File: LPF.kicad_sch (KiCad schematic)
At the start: 24 parts

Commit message: v0.6 ERC passes.  I went over it with a fine tooth comb and corrected lots of little stuff.  Ron should review all the components I have to create very carefully.  In particular, MPS-751 symbol does not look correct.
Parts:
- C15: value ? pF -> 47 pF
- C16: value ? pF -> 36 pF
- C4: value ? pF -> 220 pF
- C8: value ? pF -> 100 pF
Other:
- note added: "These are RF paths."
- title: QMX Amp -> QMX+ Amp
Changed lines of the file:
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@@
 	(paper "USLetter")
 	(title_block
-		(title "QMX Amp")
-		(date "2024-08-12")
-		(rev "v0.5")
+		(title "QMX+ Amp")
+		(date "2024-08-13")
+		(rev "v0.6")
 		(company "WA7GIL")
 	)
@@
 		)
 	)
+	(text "These are RF paths."
+		(exclude_from_sim no)
+		(at 21.59 22.098 0)
+		(effects
+			(font
+				(size 1.27 1.27)
+			)
+			(justify left)
+		)
+	)
 	(hierarchical_label "LPF0-OUT"
 		(shape output)
@@
 			)
 		)
-		(property "Value" "? pF"
+		(property "Value" "220 pF"
 			(at 129.54 26.67 90)
 			(effects
@@
 			)
 		)
-		(property "Value" "? pF"
+		(property "Value" "100 pF"
 			(at 129.54 60.96 90)
 			(effects
@@
 			)
 		)
-		(property "Value" "? pF"
+		(property "Value" "47 pF"
 			(at 130.81 95.25 90)
 			(effects
@@
 			)
 		)
-		(property "Value" "? pF"
+		(property "Value" "36 pF"
 			(at 130.81 129.54 90)
 			(effects

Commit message: I think I am working on picking parts
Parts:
- L1, L2, L3, L4, L5, L6, L7, L8: footprint (none) -> ZZZMyLibrary:Toroid_T50_Vertical_L14.0mm_W5.6mm
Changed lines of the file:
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@@
 			)
 		)
-		(property "Footprint" ""
+		(property "Footprint" "ZZZMyLibrary:Toroid_T50_Vertical_L14.0mm_W5.6mm"
 			(at 104.14 76.2 0)
 			(effects
@@
 			)
 		)
-		(property "Footprint" ""
+		(property "Footprint" "ZZZMyLibrary:Toroid_T50_Vertical_L14.0mm_W5.6mm"
 			(at 104.14 41.91 0)
 			(effects
@@
 			)
 		)
-		(property "Footprint" ""
+		(property "Footprint" "ZZZMyLibrary:Toroid_T50_Vertical_L14.0mm_W5.6mm"
 			(at 129.54 76.2 0)
 			(effects
@@
 			)
 		)
-		(property "Footprint" ""
+		(property "Footprint" "ZZZMyLibrary:Toroid_T50_Vertical_L14.0mm_W5.6mm"
 			(at 105.41 144.78 0)
 			(effects
@@
 			)
 		)
-		(property "Footprint" ""
+		(property "Footprint" "ZZZMyLibrary:Toroid_T50_Vertical_L14.0mm_W5.6mm"
 			(at 105.41 110.49 0)
 			(effects
@@
 			)
 		)
-		(property "Footprint" ""
+		(property "Footprint" "ZZZMyLibrary:Toroid_T50_Vertical_L14.0mm_W5.6mm"
 			(at 129.54 41.91 0)
 			(effects
@@
 			)
 		)
-		(property "Footprint" ""
+		(property "Footprint" "ZZZMyLibrary:Toroid_T50_Vertical_L14.0mm_W5.6mm"
 			(at 130.81 110.49 0)
 			(effects
@@
 			)
 		)
-		(property "Footprint" ""
+		(property "Footprint" "ZZZMyLibrary:Toroid_T50_Vertical_L14.0mm_W5.6mm"
 			(at 130.81 144.78 0)
 			(effects

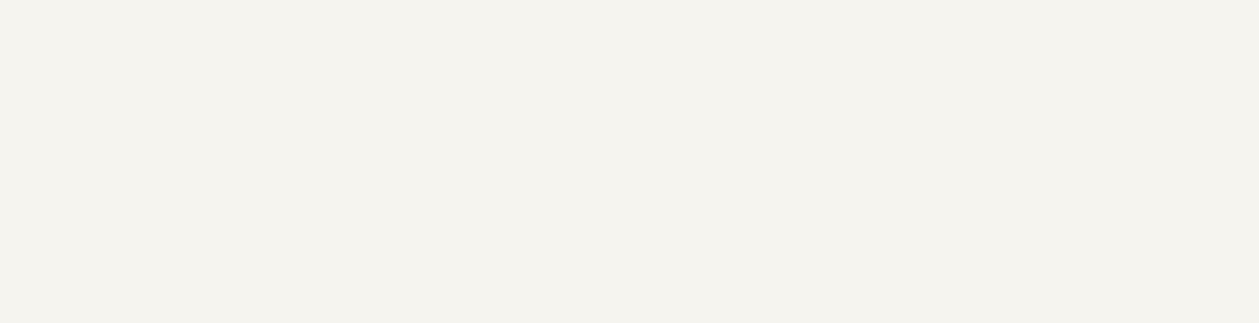
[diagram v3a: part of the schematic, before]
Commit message: created 11x4mm footprint with 5mm pin spacing for caps on LPF per Ron
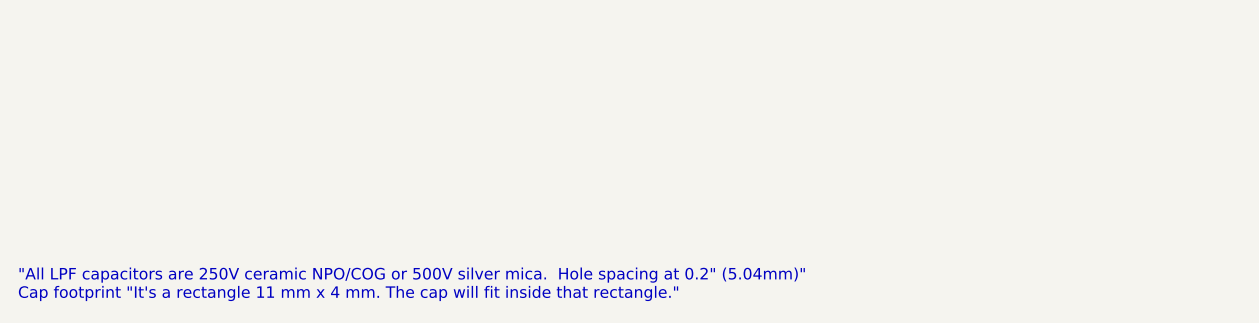
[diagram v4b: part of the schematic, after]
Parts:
- C1, C10, C11, C12, C13, C14, C15, C16, C2, C3, C4, C5, C6, C7, C8, C9: footprint (none) -> ZZZMyLibrary:C_Disc_D11.0mm_W4.0mm_P5.00mm
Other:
- note added: ""All LPF capacitors are 250V ceramic NPO/COG or 500V silver mica. Hole spacing at 0.2" (5.04mm)" Cap footprint "It's a rectangle 11 mm x 4 mm. The cap will fit inside that rectangle.""
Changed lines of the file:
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@@
 	(title_block
 		(title "QMX+ Amp")
-		(date "2024-08-13")
+		(date "2024-08-18")
 		(rev "v0.7")
 		(company "WA7GIL")
@@
 		)
 	)
+	(text "\"All LPF capacitors are 250V ceramic NPO/COG or 500V silver mica.  Hole spacing at 0.2\" (5.04mm)\"\nCap footprint \"It's a rectangle 11 mm x 4 mm. The cap will fit inside that rectangle.\""
+		(exclude_from_sim no)
+		(at 18.288 192.532 0)
+		(effects
+			(font
+				(size 1.27 1.27)
+			)
+			(justify left)
+		)
+	)
 	(hierarchical_label "LPF0-OUT"
 		(shape output)
@@
 			)
 		)
-		(property "Footprint" ""
+		(property "Footprint" "ZZZMyLibrary:C_Disc_D11.0mm_W4.0mm_P5.00mm"
 			(at 101.2952 49.53 0)
 			(effects
@@
 			)
 		)
-		(property "Footprint" ""
+		(property "Footprint" "ZZZMyLibrary:C_Disc_D11.0mm_W4.0mm_P5.00mm"
 			(at 133.35 30.7848 0)
 			(effects
@@
 			)
 		)
-		(property "Footprint" ""
+		(property "Footprint" "ZZZMyLibrary:C_Disc_D11.0mm_W4.0mm_P5.00mm"
 			(at 139.3952 49.53 0)
 			(effects
@@
 			)
 		)
-		(property "Footprint" ""
+		(property "Footprint" "ZZZMyLibrary:C_Disc_D11.0mm_W4.0mm_P5.00mm"
 			(at 121.6152 152.4 0)
 			(effects
@@
 			)
 		)
-		(property "Footprint" ""
+		(property "Footprint" "ZZZMyLibrary:C_Disc_D11.0mm_W4.0mm_P5.00mm"
 			(at 102.5652 152.4 0)
 			(effects
@@
 			)
 		)
-		(property "Footprint" ""
+		(property "Footprint" "ZZZMyLibrary:C_Disc_D11.0mm_W4.0mm_P5.00mm"
 			(at 133.35 65.0748 0)
 			(effects
@@
 			)
 		)
-		(property "Footprint" ""
+		(property "Footprint" "ZZZMyLibrary:C_Disc_D11.0mm_W4.0mm_P5.00mm"
 			(at 121.6152 118.11 0)
 			(effects
@@
 			)
 		)
-		(property "Footprint" ""
+		(property "Footprint" "ZZZMyLibrary:C_Disc_D11.0mm_W4.0mm_P5.00mm"
 			(at 134.62 99.3648 0)
 			(effects
@@
 			)
 		)
-		(property "Footprint" ""
+		(property "Footprint" "ZZZMyLibrary:C_Disc_D11.0mm_W4.0mm_P5.00mm"
 			(at 118.4148 41.91 0)
 			(effects
@@
 			)
 		)
-		(property "Footprint" ""
+		(property "Footprint" "ZZZMyLibrary:C_Disc_D11.0mm_W4.0mm_P5.00mm"
 			(at 102.5652 118.11 0)
 			(effects
@@
 			)
 		)
-		(property "Footprint" ""
+		(property "Footprint" "ZZZMyLibrary:C_Disc_D11.0mm_W4.0mm_P5.00mm"
 			(at 140.6652 152.4 0)
 			(effects
@@
 			)
 		)
-		(property "Footprint" ""
+		(property "Footprint" "ZZZMyLibrary:C_Disc_D11.0mm_W4.0mm_P5.00mm"
 			(at 101.2952 83.82 0)
 			(effects
@@
 			)
 		)
-		(property "Footprint" ""
+		(property "Footprint" "ZZZMyLibrary:C_Disc_D11.0mm_W4.0mm_P5.00mm"
 			(at 139.3952 83.82 0)
 			(effects
@@
 			)
 		)
-		(property "Footprint" ""
+		(property "Footprint" "ZZZMyLibrary:C_Disc_D11.0mm_W4.0mm_P5.00mm"
 			(at 134.62 133.6548 0)
 			(effects
@@
 			)
 		)
-		(property "Footprint" ""
+		(property "Footprint" "ZZZMyLibrary:C_Disc_D11.0mm_W4.0mm_P5.00mm"
 			(at 120.3452 83.82 0)
 			(effects
@@
 			)
 		)
-		(property "Footprint" ""
+		(property "Footprint" "ZZZMyLibrary:C_Disc_D11.0mm_W4.0mm_P5.00mm"
 			(at 140.6652 118.11 0)
 			(effects
